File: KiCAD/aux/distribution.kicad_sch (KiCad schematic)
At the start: 23 parts, among them U1 AD8055ARTZ-R2

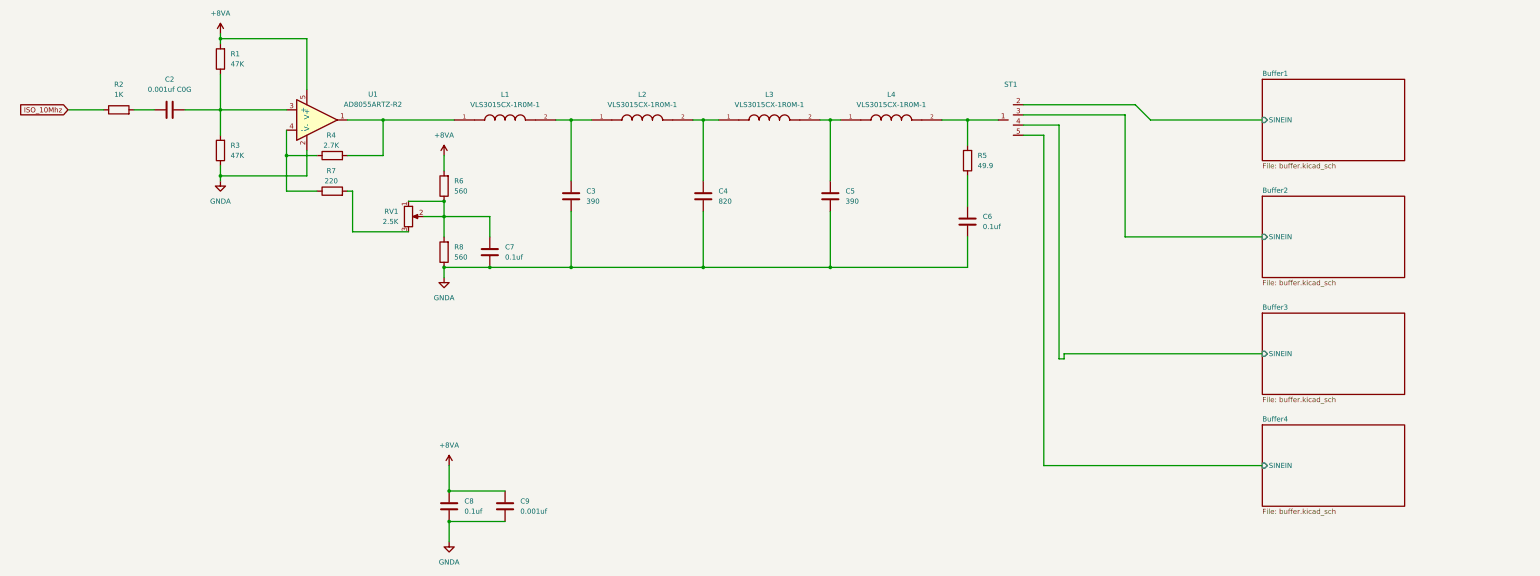
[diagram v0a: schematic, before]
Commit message: Reworked, now with IRIG option board complete
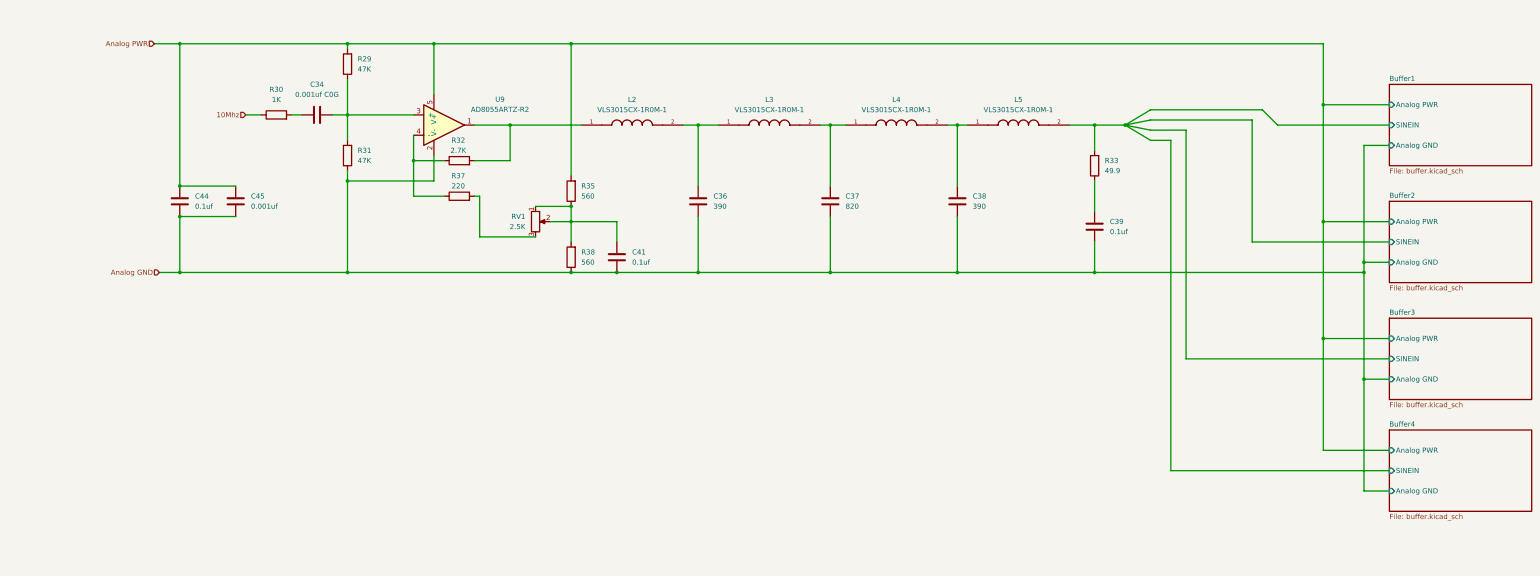
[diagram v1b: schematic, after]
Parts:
- removed ST1: ~, ! Scott:star5tie, symbol ! Scott:star5tie
- renumbered C2 to C34, C3 to C36, C4 to C37, C5 to C38, C6 to C39, C7 to C41, C8 to C44, C9 to C45, L1 to L2, L2 to L3, L3 to L4, L4 to L5, R1 to R29, R2 to R30, R3 to R31, R4 to R32, R5 to R33, R6 to R35, R7 to R37, R8 to R38, U1 to U9
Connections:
- net Buffer1/SINEIN: now also L5.2, R33.2
- net +8VA renamed Analog PWR
- net GNDA renamed Analog GND
- net ISO_10Mhz renamed 10Mhz
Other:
- sheet Buffer1 ports: added Analog GND, Analog PWR; removed none
- sheet Buffer2 ports: added Analog GND, Analog PWR; removed none
- sheet Buffer3 ports: added Analog GND, Analog PWR; removed none
- sheet Buffer4 ports: added Analog GND, Analog PWR; removed none
- moved on the sheet: C34, C36, C37, C38, C39, C41, C44, C45, L2, L3, L4, L5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
